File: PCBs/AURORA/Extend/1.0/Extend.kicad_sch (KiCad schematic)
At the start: 28 parts, among them J1 Conn_01x02_Pin, J17 Conn_01x05_Pin, J2 Conn_01x03_Pin, J20 Conn_01x02_Male, J22 Conn_01x02_Male, J23 Conn_01x03_Pin, J3 Conn_01x02_Pin, J4 Conn_01x02_Male, J5 Conn_01x02_Male, J6 Conn_01x04_Pin, J7 Conn_01x02_Male, J8 Conn_01x02_Male, J9 Conn_01x02_Pin, U1 MCP23017_SS, U2 MCP23017_SS

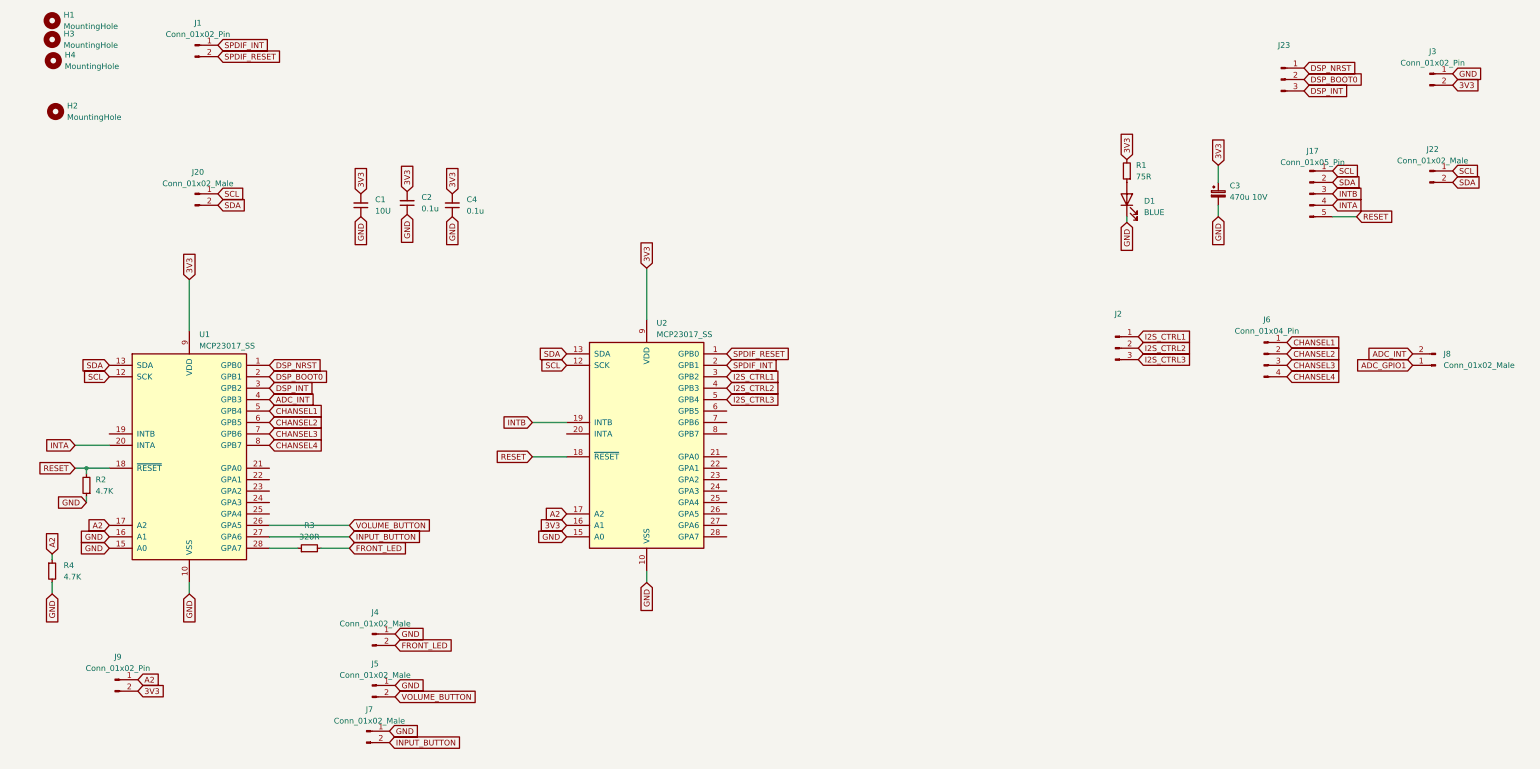
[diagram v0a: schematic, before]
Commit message: Updates to amplifer
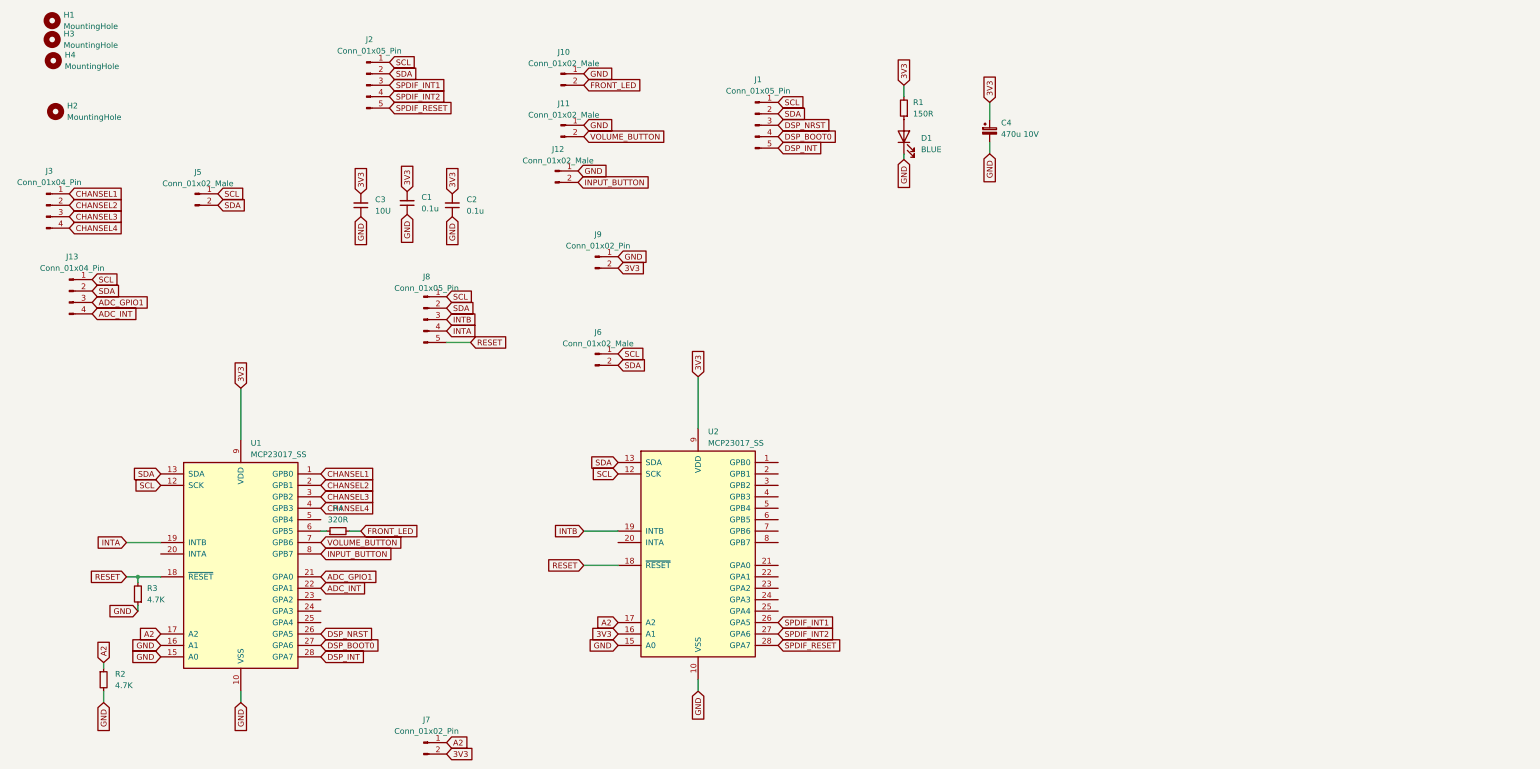
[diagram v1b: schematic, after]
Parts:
- removed J1: Conn_01x02_Pin, Connector_JST:JST_PH_B2B-PH-K_1x02_P2.00mm_Vertical, symbol Connector:Conn_01x02_Pin
- removed J2, J23: Conn_01x03_Pin, Connector_JST:JST_PH_B3B-PH-K_1x03_P2.00mm_Vertical, symbol Connector:Conn_01x03_Pin
- removed J8: Conn_01x02_Male, Connector_JST:JST_PH_B2B-PH-K_1x02_P2.00mm_Vertical, symbol Connector:Conn_01x02_Male
- removed R3: 320R, Resistor_SMD:R_0603_1608Metric_Pad0.98x0.95mm_HandSolder, symbol Device:R_Small
- added J1, J2: Conn_01x05_Pin, Connector_JST:JST_PH_B5B-PH-K_1x05_P2.00mm_Vertical, symbol Connector:Conn_01x05_Pin
- added J13: Conn_01x04_Pin, Connector_JST:JST_PH_B4B-PH-K_1x04_P2.00mm_Vertical, symbol Connector:Conn_01x04_Pin
- added R4: 320R, Resistor_SMD:R_0603_1608Metric_Pad0.98x0.95mm_HandSolder, symbol Device:R_Small
- D1: footprint LED_SMD:LED_0805_2012Metric_Pad1.15x1.40mm_HandSolder -> LED_SMD:LED_0603_1608Metric
- R1: value 75R -> 150R; footprint Resistor_SMD:R_0603_1608Metric_Pad0.98x0.95mm_HandSolder -> Resistor_SMD:R_0603_1608Metric
- renumbered C2 to C1, C4 to C2, C1 to C3, C3 to C4, J4 to J10, J5 to J11, J7 to J12, J6 to J3, J20 to J5, J22 to J6, J9 to J7, J17 to J8, J3 to J9, R4 to R2, R2 to R3
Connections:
- net ADC_GPIO1: now also U1.21 (GPA0), J13.3 (Pin_3)
- net ADC_INT: now also U1.22 (GPA1), J13.4 (Pin_4); no longer U1.4 (GPB3)
- net CHANSEL1: now also U1.1 (GPB0); no longer U1.5 (GPB4)
- net CHANSEL2: now also U1.2 (GPB1); no longer U1.6 (GPB5)
- net CHANSEL3: now also U1.3 (GPB2); no longer U1.7 (GPB6)
- net CHANSEL4: now also U1.4 (GPB3); no longer U1.8 (GPB7)
- net DSP_BOOT0: now also U1.27 (GPA6), J1.4 (Pin_4); no longer U1.2 (GPB1)
- net DSP_INT: now also U1.28 (GPA7), J1.5 (Pin_5); no longer U1.3 (GPB2)
- net DSP_NRST: now also U1.26 (GPA5), J1.3 (Pin_3); no longer U1.1 (GPB0)
- net FRONT_LED: now also R4.2
- net INPUT_BUTTON: now also U1.8 (GPB7); no longer U1.27 (GPA6)
- net INTA: now also U1.19 (INTB); no longer U1.20 (INTA)
- net SCL: now also J1.1 (Pin_1), J13.1 (Pin_1), J2.1 (Pin_1)
- net SDA: now also J1.2 (Pin_2), J13.2 (Pin_2), J2.2 (Pin_2)
- net SPDIF_RESET: now also U2.28 (GPA7), J2.5 (Pin_5); no longer U2.1 (GPB0)
- net VOLUME_BUTTON: now also U1.7 (GPB6); no longer U1.26 (GPA5)
- net SPDIF_INT1: now reaches U2.26 (GPA5)
- net SPDIF_INT1: now also J2.3 (Pin_3)
- net SPDIF_INT2: now reaches U2.27 (GPA6)
- net SPDIF_INT2: now also J2.4 (Pin_4)
- net I2S_CTRL1: no longer names the net of U2.3 (GPB2)
- net I2S_CTRL2: no longer names the net of U2.4 (GPB3)
- net I2S_CTRL3: no longer names the net of U2.5 (GPB4)
- net SPDIF_INT: no longer names the net of U2.2 (GPB1)
- new net: R4.1, U1.6 (GPB5)
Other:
- moved on the sheet: C4, D1, J10, J11, J12, J3, J6, J7, J8, J9, R1, R2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
